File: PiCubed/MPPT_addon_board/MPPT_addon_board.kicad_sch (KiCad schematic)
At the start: 16 parts, among them J1 HW-09-10-L-D-400-SM, Q9 MBT2222ADW1T1, U1 LT8491-mezzanine, U2 LT8491-mezzanine

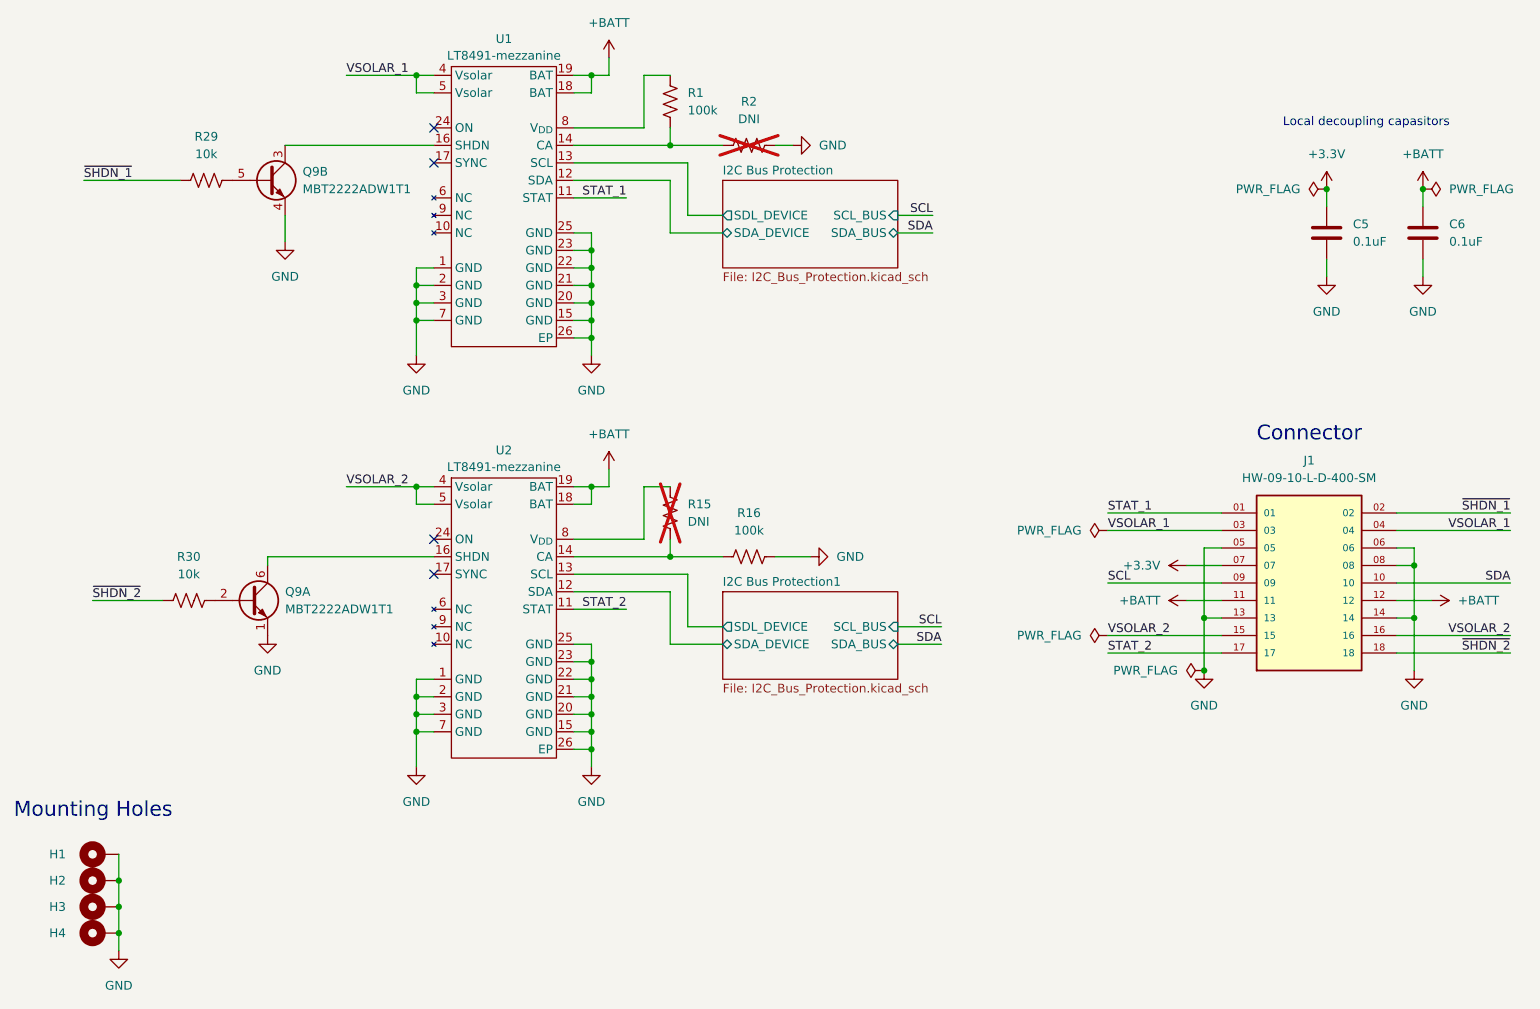
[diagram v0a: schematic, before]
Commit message: Updated MPPT add-on board to Kicad 9
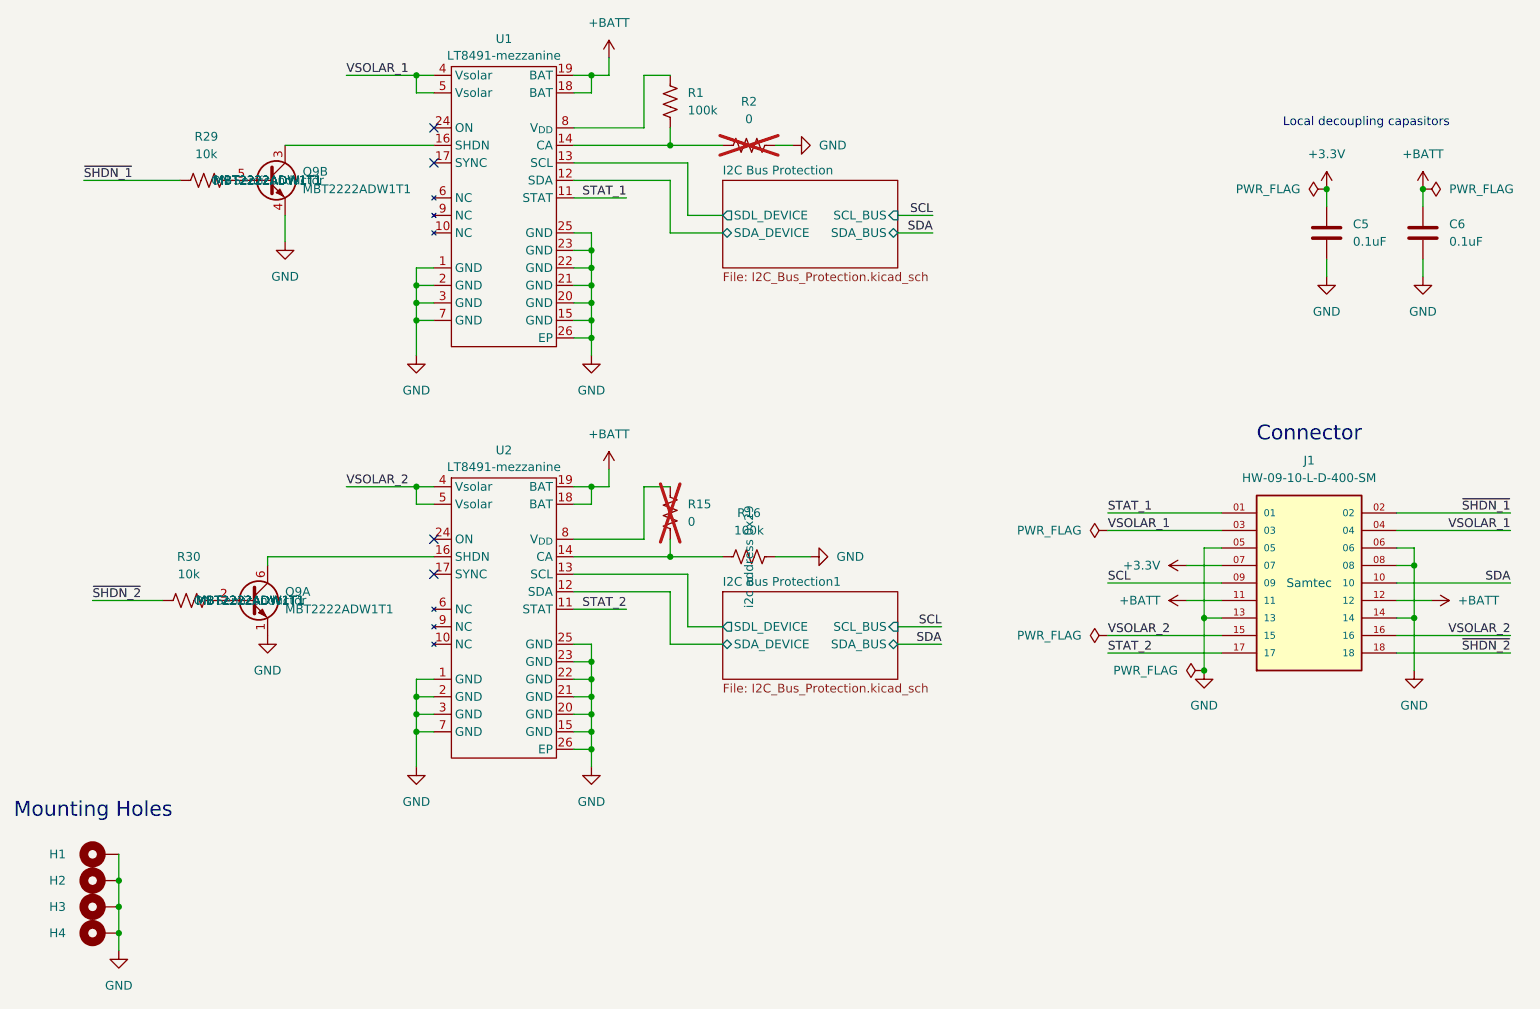
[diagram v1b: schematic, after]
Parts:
- J1: MANUFACTURER Samtec -> (none); Manufacturer_Name (none) -> Samtec; PARTREV A -> (none); STANDARD Manufacturer Recommendations -> (none)
- Q9: Flight (none) -> MBT2222ADW1T1; Manufacturer_Name (none) -> ON Semiconductor; Manufacturer_Part_Number (none) -> MBT2222ADW1T1; Proto (none) -> MBT2222ADW1T1
- R15, R2: value DNI -> 0
- R16: note (none) -> i2c address 0x29; note  i2c address 0x29 -> (none)
